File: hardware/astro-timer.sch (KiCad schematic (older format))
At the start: 26 parts, among them J1 AVR-ISP-6, J2 AudioJack3, Q1 Q_NPN_EBC, Q2 Q_NPN_EBC, SW1 SW_SPST, SW2 SW_Push, SW3 SW_Push, SW4 Rotary_Encoder_Switch, U1 ATmega328P-PU, Y1 Crystal

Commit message: SMT version
because I feel like trying out JLC's assembly service
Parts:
- removed Q1, Q2: Q_NPN_EBC, Package_TO_SOT_THT:TO-92_Inline_Wide, symbol Device:Q_NPN_EBC
- removed U1: ATmega328P-PU, Package_DIP:DIP-28_W7.62mm, symbol MCU_Microchip_ATmega:ATmega328P-PU
- added Q1, Q2: Q_NPN_BEC, Package_TO_SOT_SMD:SOT-23, symbol Device:Q_NPN_BEC
- added U1: ATmega328P-AU, Package_QFP:TQFP-32_7x7mm_P0.8mm, symbol MCU_Microchip_ATmega:ATmega328P-AU
- C1, C2: value C -> 22pF; footprint Capacitor_THT:C_Disc_D3.0mm_W2.0mm_P2.50mm -> Capacitor_SMD:C_0805_2012Metric
- C3: value C -> 100nF; footprint Capacitor_THT:C_Disc_D3.0mm_W1.6mm_P2.50mm -> Capacitor_SMD:C_0805_2012Metric
- R1, R2, R3, R4, R5, R6, R7, R8: value R -> 470; footprint Resistor_THT:R_Axial_DIN0204_L3.6mm_D1.6mm_P2.54mm_Vertical -> Resistor_SMD:R_0805_2012Metric
- R10, R9: value R -> 22K; footprint Resistor_THT:R_Axial_DIN0204_L3.6mm_D1.6mm_P2.54mm_Vertical -> Resistor_SMD:R_0805_2012Metric
- Y1: footprint Crystal:Crystal_Round_D2.0mm_Vertical -> Crystal:Crystal_SMD_3215-2Pin_3.2x1.5mm
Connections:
- no-connect marks 1 -> 3
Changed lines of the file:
@@
-$EndComp
-$Comp
-L MCU_Microchip_ATmega:ATmega328P-PU U1
-U 1 1 602EB93D
-P 4600 1950
-F 0 "U1" V 3819 1950 50  0000 C CNN
-F 1 "ATmega328P-PU" V 3910 1950 50  0000 C CNN
-F 2 "Package_DIP:DIP-28_W7.62mm" H 4600 1950 50  0001 C CIN
-F 3 "http://ww1.microchip.com/downloads/en/DeviceDoc/ATmega328_P%20AVR%20MCU%20with%20picoPower%20Technology%20Data%20Sheet%2040001984A.pdf" H 4600 1950 50  0001 C CNN
-	1    4600 1950
-	0    1    1    0
 $EndComp
 $Comp
@@
 U 1 1 6030D026
 P 4100 5100
-F 0 "R8" H 4050 5150 50  0000 L CNN
-F 1 "R" H 4050 5050 50  0000 L CNN
-F 2 "Resistor_THT:R_Axial_DIN0204_L3.6mm_D1.6mm_P2.54mm_Vertical" V 4030 5100 50  0001 C CNN
+F 0 "R8" V 4100 5200 50  0000 L CNN
+F 1 "470" V 4100 5050 50  0000 L CNN
+F 2 "Resistor_SMD:R_0805_2012Metric" V 4030 5100 50  0001 C CNN
 F 3 "~" H 4100 5100 50  0001 C CNN
 	1    4100 5100
@@
 U 1 1 6030D793
 P 4000 5100
-F 0 "R7" H 3950 5150 50  0000 L CNN
-F 1 "R" H 3950 5050 50  0000 L CNN
-F 2 "Resistor_THT:R_Axial_DIN0204_L3.6mm_D1.6mm_P2.54mm_Vertical" V 3930 5100 50  0001 C CNN
+F 0 "R7" V 4000 5200 50  0000 L CNN
+F 1 "470" V 4000 5050 50  0000 L CNN
+F 2 "Resistor_SMD:R_0805_2012Metric" V 3930 5100 50  0001 C CNN
 F 3 "~" H 4000 5100 50  0001 C CNN
 	1    4000 5100
@@
 U 1 1 6030D9D4
 P 3900 5100
-F 0 "R6" H 3850 5150 50  0000 L CNN
-F 1 "R" H 3850 5050 50  0000 L CNN
-F 2 "Resistor_THT:R_Axial_DIN0204_L3.6mm_D1.6mm_P2.54mm_Vertical" V 3830 5100 50  0001 C CNN
+F 0 "R6" V 3900 5200 50  0000 L CNN
+F 1 "470" V 3900 5050 50  0000 L CNN
+F 2 "Resistor_SMD:R_0805_2012Metric" V 3830 5100 50  0001 C CNN
 F 3 "~" H 3900 5100 50  0001 C CNN
 	1    3900 5100
@@
 U 1 1 6030DC01
 P 3800 5100
-F 0 "R5" H 3750 5150 50  0000 L CNN
-F 1 "R" H 3750 5050 50  0000 L CNN
-F 2 "Resistor_THT:R_Axial_DIN0204_L3.6mm_D1.6mm_P2.54mm_Vertical" V 3730 5100 50  0001 C CNN
+F 0 "R5" V 3800 5200 50  0000 L CNN
+F 1 "470" V 3800 5050 50  0000 L CNN
+F 2 "Resistor_SMD:R_0805_2012Metric" V 3730 5100 50  0001 C CNN
 F 3 "~" H 3800 5100 50  0001 C CNN
 	1    3800 5100
@@
 U 1 1 6030DD77
 P 3700 5100
-F 0 "R4" H 3650 5150 50  0000 L CNN
-F 1 "R" H 3650 5050 50  0000 L CNN
-F 2 "Resistor_THT:R_Axial_DIN0204_L3.6mm_D1.6mm_P2.54mm_Vertical" V 3630 5100 50  0001 C CNN
+F 0 "R4" V 3700 5200 50  0000 L CNN
+F 1 "470" V 3700 5050 50  0000 L CNN
+F 2 "Resistor_SMD:R_0805_2012Metric" V 3630 5100 50  0001 C CNN
 F 3 "~" H 3700 5100 50  0001 C CNN
 	1    3700 5100
@@
 U 1 1 6030DF7F
 P 3600 5100
-F 0 "R3" H 3550 5150 50  0000 L CNN
-F 1 "R" H 3550 5050 50  0000 L CNN
-F 2 "Resistor_THT:R_Axial_DIN0204_L3.6mm_D1.6mm_P2.54mm_Vertical" V 3530 5100 50  0001 C CNN
+F 0 "R3" V 3600 5200 50  0000 L CNN
+F 1 "470" V 3600 5050 50  0000 L CNN
+F 2 "Resistor_SMD:R_0805_2012Metric" V 3530 5100 50  0001 C CNN
 F 3 "~" H 3600 5100 50  0001 C CNN
 	1    3600 5100
@@
 U 1 1 6030E0EA
 P 3500 5100
-F 0 "R2" H 3450 5150 50  0000 L CNN
-F 1 "R" H 3450 5050 50  0000 L CNN
-F 2 "Resistor_THT:R_Axial_DIN0204_L3.6mm_D1.6mm_P2.54mm_Vertical" V 3430 5100 50  0001 C CNN
+F 0 "R2" V 3500 5200 50  0000 L CNN
+F 1 "470" V 3500 5050 50  0000 L CNN
+F 2 "Resistor_SMD:R_0805_2012Metric" V 3430 5100 50  0001 C CNN
 F 3 "~" H 3500 5100 50  0001 C CNN
 	1    3500 5100
-	1    0    0    -1
-$EndComp
-$Comp
-L Device:R R1
-U 1 1 6030E316
-P 3400 5100
-F 0 "R1" H 3350 5150 50  0000 L CNN
-F 1 "R" H 3350 5050 50  0000 L CNN
-F 2 "Resistor_THT:R_Axial_DIN0204_L3.6mm_D1.6mm_P2.54mm_Vertical" V 3330 5100 50  0001 C CNN
-F 3 "~" H 3400 5100 50  0001 C CNN
-	1    3400 5100
 	1    0    0    -1
 $EndComp
@@
 P 7850 4450
 F 0 "R9" V 7643 4450 50  0000 C CNN
-F 1 "R" V 7734 4450 50  0000 C CNN
-F 2 "Resistor_THT:R_Axial_DIN0204_L3.6mm_D1.6mm_P2.54mm_Vertical" V 7780 4450 50  0001 C CNN
+F 1 "22K" V 7734 4450 50  0000 C CNN
+F 2 "Resistor_SMD:R_0805_2012Metric" V 7780 4450 50  0001 C CNN
 F 3 "~" H 7850 4450 50  0001 C CNN
 	1    7850 4450
@@
 P 6200 2200
 F 0 "C3" H 6315 2246 50  0000 L CNN
-F 1 "C" H 6315 2155 50  0000 L CNN
-F 2 "Capacitor_THT:C_Disc_D3.0mm_W1.6mm_P2.50mm" H 6238 2050 50  0001 C CNN
+F 1 "100nF" H 6315 2155 50  0000 L CNN
+F 2 "Capacitor_SMD:C_0805_2012Metric" H 6238 2050 50  0001 C CNN
 F 3 "~" H 6200 2200 50  0001 C CNN
 	1    6200 2200
@@
 F 0 "Y1" H 5050 3868 50  0000 C CNN
 F 1 "Crystal" H 5050 3777 50  0000 C CNN
-F 2 "Crystal:Crystal_Round_D2.0mm_Vertical" H 5050 3600 50  0001 C CNN
+F 2 "Crystal:Crystal_SMD_3215-2Pin_3.2x1.5mm" H 5050 3600 50  0001 C CNN
 F 3 "~" H 5050 3600 50  0001 C CNN
 	1    5050 3600
@@
 P 4850 3850
 F 0 "C1" H 4965 3896 50  0000 L CNN
-F 1 "C" H 4965 3805 50  0000 L CNN
-F 2 "Capacitor_THT:C_Disc_D3.0mm_W2.0mm_P2.50mm" H 4888 3700 50  0001 C CNN
+F 1 "22pF" H 4965 3805 50  0000 L CNN
+F 2 "Capacitor_SMD:C_0805_2012Metric" H 4888 3700 50  0001 C CNN
 F 3 "~" H 4850 3850 50  0001 C CNN
 	1    4850 3850
@@
 P 5200 3850
 F 0 "C2" H 5315 3896 50  0000 L CNN
-F 1 "C" H 5315 3805 50  0000 L CNN
-F 2 "Capacitor_THT:C_Disc_D3.0mm_W2.0mm_P2.50mm" H 5238 3700 50  0001 C CNN
+F 1 "22pF" H 5315 3805 50  0000 L CNN
+F 2 "Capacitor_SMD:C_0805_2012Metric" H 5238 3700 50  0001 C CNN
 F 3 "~" H 5200 3850 50  0001 C CNN
 	1    5200 3850
@@
 P 7850 5200
 F 0 "R10" V 7643 5200 50  0000 C CNN
-F 1 "R" V 7734 5200 50  0000 C CNN
-F 2 "Resistor_THT:R_Axial_DIN0204_L3.6mm_D1.6mm_P2.54mm_Vertical" V 7780 5200 50  0001 C CNN
+F 1 "22K" V 7734 5200 50  0000 C CNN
+F 2 "Resistor_SMD:R_0805_2012Metric" V 7780 5200 50  0001 C CNN
 F 3 "~" H 7850 5200 50  0001 C CNN
 	1    7850 5200
 	0    1    1    0
-$EndComp
-$Comp
-L Device:Q_NPN_EBC Q2
-U 1 1 604C56C8
-P 8200 5200
-F 0 "Q2" H 8391 5246 50  0000 L CNN
-F 1 "Q_NPN_EBC" H 8391 5155 50  0000 L CNN
-F 2 "Package_TO_SOT_THT:TO-92_Inline_Wide" H 8400 5300 50  0001 C CNN
-F 3 "~" H 8200 5200 50  0001 C CNN
-	1    8200 5200
-	1    0    0    -1
-$EndComp
-$Comp
-L Device:Q_NPN_EBC Q1
-U 1 1 604C6439
-P 8200 4450
-F 0 "Q1" H 8391 4496 50  0000 L CNN
-F 1 "Q_NPN_EBC" H 8391 4405 50  0000 L CNN
-F 2 "Package_TO_SOT_THT:TO-92_Inline_Wide" H 8400 4550 50  0001 C CNN
-F 3 "~" H 8200 4450 50  0001 C CNN
-	1    8200 4450
-	1    0    0    -1
 $EndComp
 Wire Wire Line
@@
 Wire Wire Line
 	4400 4150 4400 2550
+$Comp
+L Device:R R1
+U 1 1 6030E316
+P 3400 5100
+F 0 "R1" V 3400 5200 50  0000 L CNN
+F 1 "470" V 3400 5050 50  0000 L CNN
+F 2 "Resistor_SMD:R_0805_2012Metric" V 3330 5100 50  0001 C CNN
+F 3 "~" H 3400 5100 50  0001 C CNN
+	1    3400 5100
+	1    0    0    -1
+$EndComp
+$Comp
+L MCU_Microchip_ATmega:ATmega328P-AU U1
+U 1 1 604F6DD0
+P 4600 1950
+F 0 "U1" V 4554 407 50  0000 R CNN
+F 1 "ATmega328P-AU" V 4645 407 50  0000 R CNN
+F 2 "Package_QFP:TQFP-32_7x7mm_P0.8mm" H 4600 1950 50  0001 C CIN
+F 3 "http://ww1.microchip.com/downloads/en/DeviceDoc/ATmega328_P%20AVR%20MCU%20with%20picoPower%20Technology%20Data%20Sheet%2040001984A.pdf" H 4600 1950 50  0001 C CNN
+	1    4600 1950
+	0    1    1    0
+$EndComp
+NoConn ~ 5500 1350
+NoConn ~ 5600 1350
+$Comp
+L Device:Q_NPN_BEC Q1
+U 1 1 6056E7E2
+P 8200 4450
+F 0 "Q1" H 8391 4496 50  0000 L CNN
+F 1 "Q_NPN_BEC" H 8391 4405 50  0000 L CNN
+F 2 "Package_TO_SOT_SMD:SOT-23" H 8400 4550 50  0001 C CNN
+F 3 "~" H 8200 4450 50  0001 C CNN
+	1    8200 4450
+	1    0    0    -1
+$EndComp
+$Comp
+L Device:Q_NPN_BEC Q2
+U 1 1 6056EC54
+P 8200 5200
+F 0 "Q2" H 8391 5246 50  0000 L CNN
+F 1 "Q_NPN_BEC" H 8391 5155 50  0000 L CNN
+F 2 "Package_TO_SOT_SMD:SOT-23" H 8400 5300 50  0001 C CNN
+F 3 "~" H 8200 5200 50  0001 C CNN
+	1    8200 5200
+	1    0    0    -1
+$EndComp
 $EndSCHEMATC

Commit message: jlc part numbers
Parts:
- C1, C2: JLC (none) -> C1804
- Q1, Q2: JLC (none) -> C6749
- R1, R2, R3, R4, R5, R6, R7, R8: JLC (none) -> C17710
- R10, R9: JLC (none) -> C17560
- U1: JLC (none) -> C14877
- Y1: JLC (none) -> C32346
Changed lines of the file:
@@
 F 2 "Resistor_SMD:R_0805_2012Metric" V 4030 5100 50  0001 C CNN
 F 3 "~" H 4100 5100 50  0001 C CNN
+F 4 "C17710" V 4100 5100 50  0001 C CNN "JLC"
 	1    4100 5100
 	1    0    0    -1
@@
 F 2 "Resistor_SMD:R_0805_2012Metric" V 3930 5100 50  0001 C CNN
 F 3 "~" H 4000 5100 50  0001 C CNN
+F 4 "C17710" V 4000 5100 50  0001 C CNN "JLC"
 	1    4000 5100
 	1    0    0    -1
@@
 F 2 "Resistor_SMD:R_0805_2012Metric" V 3830 5100 50  0001 C CNN
 F 3 "~" H 3900 5100 50  0001 C CNN
+F 4 "C17710" V 3900 5100 50  0001 C CNN "JLC"
 	1    3900 5100
 	1    0    0    -1
@@
 F 2 "Resistor_SMD:R_0805_2012Metric" V 3730 5100 50  0001 C CNN
 F 3 "~" H 3800 5100 50  0001 C CNN
+F 4 "C17710" V 3800 5100 50  0001 C CNN "JLC"
 	1    3800 5100
 	1    0    0    -1
@@
 F 2 "Resistor_SMD:R_0805_2012Metric" V 3630 5100 50  0001 C CNN
 F 3 "~" H 3700 5100 50  0001 C CNN
+F 4 "C17710" V 3700 5100 50  0001 C CNN "JLC"
 	1    3700 5100
 	1    0    0    -1
@@
 F 2 "Resistor_SMD:R_0805_2012Metric" V 3530 5100 50  0001 C CNN
 F 3 "~" H 3600 5100 50  0001 C CNN
+F 4 "C17710" V 3600 5100 50  0001 C CNN "JLC"
 	1    3600 5100
 	1    0    0    -1
@@
 F 2 "Resistor_SMD:R_0805_2012Metric" V 3430 5100 50  0001 C CNN
 F 3 "~" H 3500 5100 50  0001 C CNN
+F 4 "C17710" V 3500 5100 50  0001 C CNN "JLC"
 	1    3500 5100
 	1    0    0    -1
@@
 F 2 "Resistor_SMD:R_0805_2012Metric" V 7780 4450 50  0001 C CNN
 F 3 "~" H 7850 4450 50  0001 C CNN
+F 4 "C17560" V 7850 4450 50  0001 C CNN "JLC"
 	1    7850 4450
 	0    1    1    0
@@
 F 2 "Crystal:Crystal_SMD_3215-2Pin_3.2x1.5mm" H 5050 3600 50  0001 C CNN
 F 3 "~" H 5050 3600 50  0001 C CNN
+F 4 "C32346" H 5050 3600 50  0001 C CNN "JLC"
 	1    5050 3600
 	1    0    0    -1
@@
 F 2 "Capacitor_SMD:C_0805_2012Metric" H 4888 3700 50  0001 C CNN
 F 3 "~" H 4850 3850 50  0001 C CNN
+F 4 "C1804" H 4850 3850 50  0001 C CNN "JLC"
 	1    4850 3850
 	1    0    0    -1
@@
 F 2 "Capacitor_SMD:C_0805_2012Metric" H 5238 3700 50  0001 C CNN
 F 3 "~" H 5200 3850 50  0001 C CNN
+F 4 "C1804" H 5200 3850 50  0001 C CNN "JLC"
 	1    5200 3850
 	1    0    0    -1
@@
 F 2 "Resistor_SMD:R_0805_2012Metric" V 7780 5200 50  0001 C CNN
 F 3 "~" H 7850 5200 50  0001 C CNN
+F 4 "C17560" V 7850 5200 50  0001 C CNN "JLC"
 	1    7850 5200
 	0    1    1    0
@@
 F 2 "Resistor_SMD:R_0805_2012Metric" V 3330 5100 50  0001 C CNN
 F 3 "~" H 3400 5100 50  0001 C CNN
+F 4 "C17710" V 3400 5100 50  0001 C CNN "JLC"
 	1    3400 5100
 	1    0    0    -1
@@
 F 2 "Package_QFP:TQFP-32_7x7mm_P0.8mm" H 4600 1950 50  0001 C CIN
 F 3 "http://ww1.microchip.com/downloads/en/DeviceDoc/ATmega328_P%20AVR%20MCU%20with%20picoPower%20Technology%20Data%20Sheet%2040001984A.pdf" H 4600 1950 50  0001 C CNN
+F 4 "C14877" V 4600 1950 50  0001 C CNN "JLC"
 	1    4600 1950
 	0    1    1    0
@@
 F 2 "Package_TO_SOT_SMD:SOT-23" H 8400 4550 50  0001 C CNN
 F 3 "~" H 8200 4450 50  0001 C CNN
+F 4 "C6749" H 8200 4450 50  0001 C CNN "JLC"
 	1    8200 4450
 	1    0    0    -1
@@
 F 2 "Package_TO_SOT_SMD:SOT-23" H 8400 5300 50  0001 C CNN
 F 3 "~" H 8200 5200 50  0001 C CNN
+F 4 "C6749" H 8200 5200 50  0001 C CNN "JLC"
 	1    8200 5200
 	1    0    0    -1

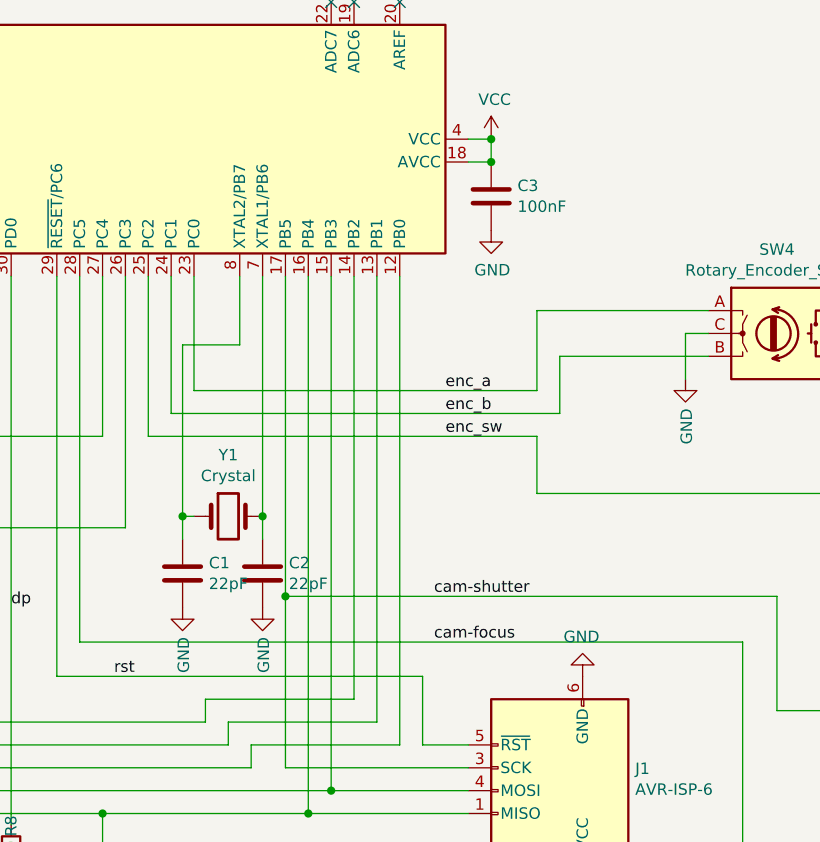
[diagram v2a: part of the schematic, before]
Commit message: fix QFN clearance and use THT crystal
JLC doesn't have a suitable one

and the load capacitors aren't needed if a 6pf crystal is used
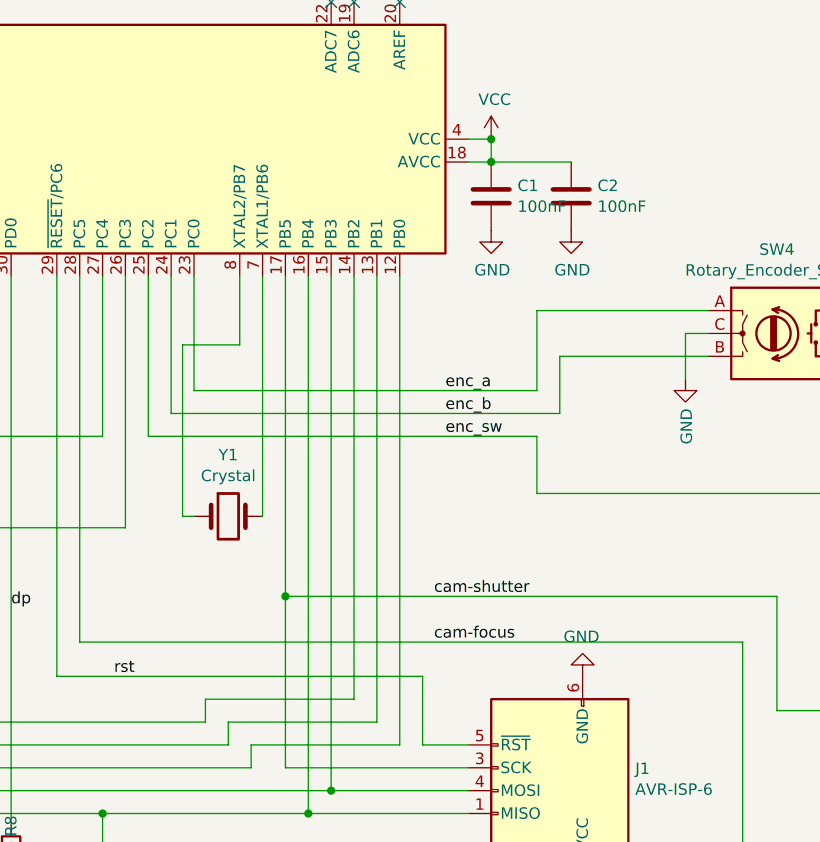
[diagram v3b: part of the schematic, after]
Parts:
- removed C1: 22pF, Capacitor_SMD:C_0805_2012Metric, symbol Device:C
- C1: renamed from C3; JLC (none) -> C49678
- C2: value 22pF -> 100nF; JLC C1804 -> C49678
- Y1: footprint Crystal:Crystal_SMD_3215-2Pin_3.2x1.5mm -> Crystal:Crystal_Round_D2.0mm_Vertical; JLC C32346 -> (none)
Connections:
- net VCC: now also C2.1
- net at U1.7 (XTAL1/PB6), Y1.2: no longer C2.1
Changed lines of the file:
@@
 $EndComp
 $Comp
-L power:GND #PWR013
+L power:GND #PWR012
 U 1 1 6033DA78
 P 8650 5400
-F 0 "#PWR013" H 8650 5150 50  0001 C CNN
+F 0 "#PWR012" H 8650 5150 50  0001 C CNN
 F 1 "GND" H 8655 5227 50  0000 C CNN
 F 2 "" H 8650 5400 50  0001 C CNN
@@
 $EndComp
 $Comp
-L power:VCC #PWR07
+L power:VCC #PWR05
 U 1 1 60347E38
 P 6200 1950
-F 0 "#PWR07" H 6200 1800 50  0001 C CNN
+F 0 "#PWR05" H 6200 1800 50  0001 C CNN
 F 1 "VCC" H 6215 2123 50  0000 C CNN
 F 2 "" H 6200 1950 50  0001 C CNN
@@
 $EndComp
 $Comp
-L power:VCC #PWR010
+L power:VCC #PWR09
 U 1 1 603488D1
 P 6600 5200
-F 0 "#PWR010" H 6600 5050 50  0001 C CNN
+F 0 "#PWR09" H 6600 5050 50  0001 C CNN
 F 1 "VCC" H 6615 5373 50  0000 C CNN
 F 2 "" H 6600 5200 50  0001 C CNN
@@
 Connection ~ 4500 4900
 $Comp
-L Device:C C3
+L Device:C C1
 U 1 1 605272F0
 P 6200 2200
-F 0 "C3" H 6315 2246 50  0000 L CNN
+F 0 "C1" H 6315 2246 50  0000 L CNN
 F 1 "100nF" H 6315 2155 50  0000 L CNN
 F 2 "Capacitor_SMD:C_0805_2012Metric" H 6238 2050 50  0001 C CNN
 F 3 "~" H 6200 2200 50  0001 C CNN
+F 4 "C49678" H 6200 2200 50  0001 C CNN "JLC"
 	1    6200 2200
 	1    0    0    -1
 $EndComp
 $Comp
-L power:GND #PWR08
+L power:GND #PWR06
 U 1 1 60528475
 P 6200 2350
-F 0 "#PWR08" H 6200 2100 50  0001 C CNN
+F 0 "#PWR06" H 6200 2100 50  0001 C CNN
 F 1 "GND" H 6205 2177 50  0000 C CNN
 F 2 "" H 6200 2350 50  0001 C CNN
@@
 	4700 3250 6400 3250
 $Comp
-L power:GND #PWR012
+L power:GND #PWR011
 U 1 1 60408112
 P 7750 3050
-F 0 "#PWR012" H 7750 2800 50  0001 C CNN
+F 0 "#PWR011" H 7750 2800 50  0001 C CNN
 F 1 "GND" H 7755 2877 50  0000 C CNN
 F 2 "" H 7750 3050 50  0001 C CNN
@@
 $EndComp
 $Comp
-L power:GND #PWR011
+L power:GND #PWR010
 U 1 1 60431874
 P 7050 3000
-F 0 "#PWR011" H 7050 2750 50  0001 C CNN
+F 0 "#PWR010" H 7050 2750 50  0001 C CNN
 F 1 "GND" V 7055 2872 50  0000 R CNN
 F 2 "" H 7050 3000 50  0001 C CNN
@@
 F 0 "Y1" H 5050 3868 50  0000 C CNN
 F 1 "Crystal" H 5050 3777 50  0000 C CNN
-F 2 "Crystal:Crystal_SMD_3215-2Pin_3.2x1.5mm" H 5050 3600 50  0001 C CNN
+F 2 "Crystal:Crystal_Round_D2.0mm_Vertical" H 5050 3600 50  0001 C CNN
 F 3 "~" H 5050 3600 50  0001 C CNN
-F 4 "C32346" H 5050 3600 50  0001 C CNN "JLC"
 	1    5050 3600
 	1    0    0    -1
@@
 Wire Wire Line
 	4900 3600 4850 3600
-Wire Wire Line
-	4850 3600 4850 3700
-Connection ~ 4850 3600
-Wire Wire Line
-	5200 3600 5200 3700
-Connection ~ 5200 3600
-$Comp
-L Device:C C1
-U 1 1 6041BDCC
-P 4850 3850
-F 0 "C1" H 4965 3896 50  0000 L CNN
-F 1 "22pF" H 4965 3805 50  0000 L CNN
-F 2 "Capacitor_SMD:C_0805_2012Metric" H 4888 3700 50  0001 C CNN
-F 3 "~" H 4850 3850 50  0001 C CNN
-F 4 "C1804" H 4850 3850 50  0001 C CNN "JLC"
-	1    4850 3850
-	1    0    0    -1
-$EndComp
-$Comp
-L Device:C C2
-U 1 1 6041C3F5
-P 5200 3850
-F 0 "C2" H 5315 3896 50  0000 L CNN
-F 1 "22pF" H 5315 3805 50  0000 L CNN
-F 2 "Capacitor_SMD:C_0805_2012Metric" H 5238 3700 50  0001 C CNN
-F 3 "~" H 5200 3850 50  0001 C CNN
-F 4 "C1804" H 5200 3850 50  0001 C CNN "JLC"
-	1    5200 3850
-	1    0    0    -1
-$EndComp
-$Comp
-L power:GND #PWR05
-U 1 1 6041CA29
-P 4850 4000
-F 0 "#PWR05" H 4850 3750 50  0001 C CNN
-F 1 "GND" V 4855 3872 50  0000 R CNN
-F 2 "" H 4850 4000 50  0001 C CNN
-F 3 "" H 4850 4000 50  0001 C CNN
-	1    4850 4000
-	1    0    0    -1
-$EndComp
-$Comp
-L power:GND #PWR06
-U 1 1 6041D3F2
-P 5200 4000
-F 0 "#PWR06" H 5200 3750 50  0001 C CNN
-F 1 "GND" V 5205 3872 50  0000 R CNN
-F 2 "" H 5200 4000 50  0001 C CNN
-F 3 "" H 5200 4000 50  0001 C CNN
-	1    5200 4000
-	1    0    0    -1
-$EndComp
 Wire Wire Line
 	4100 5250 4100 5350
@@
 	7300 5200 7700 5200
 $Comp
-L power:GND #PWR09
+L power:GND #PWR08
 U 1 1 60349F89
 P 6600 4300
-F 0 "#PWR09" H 6600 4050 50  0001 C CNN
+F 0 "#PWR08" H 6600 4050 50  0001 C CNN
 F 1 "GND" H 6605 4127 50  0000 C CNN
 F 2 "" H 6600 4300 50  0001 C CNN
@@
 	1    0    0    -1
 $EndComp
+$Comp
+L Device:C C2
+U 1 1 60556B9F
+P 6550 2200
+F 0 "C2" H 6665 2246 50  0000 L CNN
+F 1 "100nF" H 6665 2155 50  0000 L CNN
+F 2 "Capacitor_SMD:C_0805_2012Metric" H 6588 2050 50  0001 C CNN
+F 3 "~" H 6550 2200 50  0001 C CNN
+F 4 "C49678" H 6550 2200 50  0001 C CNN "JLC"
+	1    6550 2200
+	1    0    0    -1
+$EndComp
+Wire Wire Line
+	6550 2050 6200 2050
+$Comp
+L power:GND #PWR07
+U 1 1 6055A060
+P 6550 2350
+F 0 "#PWR07" H 6550 2100 50  0001 C CNN
+F 1 "GND" H 6555 2177 50  0000 C CNN
+F 2 "" H 6550 2350 50  0001 C CNN
+F 3 "" H 6550 2350 50  0001 C CNN
+	1    6550 2350
+	1    0    0    -1
+$EndComp
